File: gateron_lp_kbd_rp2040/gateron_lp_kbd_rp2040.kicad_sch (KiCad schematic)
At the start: 241 parts, among them J1 TYPE-C-31-M-12, J2 JST-SH-2 SM02B, Q1 DMG3415U, SW1 KS-33, SW10 KS-33, SW11 KS-33, SW12 KS-33, SW13 KS-33, SW14 KS-33, SW15 KS-33, SW16 KS-33, SW17 KS-33, SW18 KS-33, SW19 KS-33, SW2 KS-33, SW20 KS-33, SW21 KS-33, SW22 KS-33, SW23 KS-33, SW24 KS-33, SW25 KS-33, SW26 KS-33, SW27 KS-33, SW28 KS-33, SW29 KS-33, SW3 KS-33, SW30 KS-33, SW31 KS-33, SW32 KS-33, SW33 KS-33, SW34 KS-33, SW35 KS-33, SW36 KS-33, SW37 KS-33, SW38 KS-33, SW39 KS-33, SW4 KS-33, SW40 KS-33, SW41 KS-33, SW42 KS-33, SW43 KS-33, SW44 KS-33, SW45 KS-33, SW46 KS-33, SW47 KS-33, SW48 KS-33, SW49 KS-33, SW5 KS-33, SW50 KS-33, SW51 KS-33, SW52 KS-33, SW53 KS-33, SW54 2U, SW55 KS-33, SW56 KS-33, SW57 KS-33, SW58 KS-33, SW59 KS-33, SW6 KS-33, SW60 RESET, SW61 BOOTSEL (VERIFY), SW62 PWR MSK-12C02, SW7 KS-33, SW8 KS-33, SW9 KS-33, U1 RP2040, U2 MCP73831-2ACI/OT, U3 AP2112K-3.3, U4 USBLC6-2SC6, U5 W25Q16JVUXIQ, U6 CYW43439, U7 SN74AHCT1G125DBVR, Y1 12MHz, Y2 37.4MHz

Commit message: Verify RGB power budget against the SK6812MINI-E datasheet, fix 2 gaps
Replaced the vague "several amps" claim with a calculated figure: the
datasheet (Dongguan Opsco, SPC/SK6812MINI-E Rev. 02) confirms 12mA/channel
x 3 channels = 36mA/LED at full white, so 59 LEDs = 2.12A max -- and
surfaced two things that weren't previously flagged:

- D60 (B5819W Schottky, ~1A average current rating) sits in the VSYS path
  whenever the board is USB-powered, and 2.12A would exceed it by >2x.
  The AP2112K-3.3 LDO mismatch was already documented and correctly
  avoided by feeding the RGB chain from VSYS instead -- but D60 is NOT
  bypassed by that design, and nothing previously checked its rating
  against the real max RGB current.
- SK6812MINI-E's own datasheet specs VDD 3.7-5.5V. VSYS (a single-cell
  Li-ion rail) can sag below 3.7V well within normal discharge range, not
  just as a battery-dead edge case. The level shifter (verified
  separately) only guarantees the DIN logic threshold is met -- it says
  nothing about whether the LEDs' own supply voltage stays in spec.

Also added a local 100nF decoupling cap per LED (C100-C158, +4mm offset,
clear of the LED's own courtyard and the switch courtyards above/below),
matching the SK6812MINI-E datasheet's own typical application circuit
("even the capacitance between beads is essential") -- an earlier version
had only one bulk cap (C19) at the chain's start, 59 LEDs away from the
far end.

Verified via kicad-happy analyzers: zero new courtyard collisions, zero
schematic label collisions across the full file, only pre-existing/
expected findings remain.

Co-Authored-By: Claude Sonnet 5 <noreply@anthropic.com>
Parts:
- added C100, C101, C102, C103, C104, C105, C106, C107, C108, C109, C110, C111, C112, C113, C114, C115, C116, C117, C118, C119, C120, C121, C122, C123, C124, C125, C126, C127, C128, C129, C130, C131, C132, C133, C134, C135, C136, C137, C138, C139, C140, C141, C142, C143, C144, C145, C146, C147, C148, C149, C150, C151, C152, C153, C154, C155, C156, C157, C158: 100n, kbd:RC_0603, symbol kbd:C_kbd
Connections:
- net GND: now also C100.2, C101.2, C102.2, C103.2, C104.2, C105.2, C106.2, C107.2, C108.2, C109.2, C110.2, C111.2, C112.2, C113.2, C114.2, C115.2, C116.2, C117.2, C118.2, C119.2, C120.2, C121.2, C122.2, C123.2, C124.2, C125.2, C126.2, C127.2, C128.2, C129.2, C130.2, C131.2, C132.2, C133.2, C134.2, C135.2, C136.2, C137.2, C138.2, C139.2, C140.2, C141.2, C142.2, C143.2, C144.2, C145.2, C146.2, C147.2, C148.2, C149.2, C150.2, C151.2, C152.2, C153.2, C154.2, C155.2, C156.2, C157.2, C158.2
- net VSYS: now also C100.1, C101.1, C102.1, C103.1, C104.1, C105.1, C106.1, C107.1, C108.1, C109.1, C110.1, C111.1, C112.1, C113.1, C114.1, C115.1, C116.1, C117.1, C118.1, C119.1, C120.1, C121.1, C122.1, C123.1, C124.1, C125.1, C126.1, C127.1, C128.1, C129.1, C130.1, C131.1, C132.1, C133.1, C134.1, C135.1, C136.1, C137.1, C138.1, C139.1, C140.1, C141.1, C142.1, C143.1, C144.1, C145.1, C146.1, C147.1, C148.1, C149.1, C150.1, C151.1, C152.1, C153.1, C154.1, C155.1, C156.1, C157.1, C158.1
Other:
- note added: "RGB power budget (calculated from the SK6812MINI-E datasheet, 12mA/channel x 3 x 59 LEDs = 2.12A max at full white): fed from VSYS, NOT the 3.3V LDO (AP2112K-3.3 isn't remotely rated for this). D60 (B5819W, ~1A avg rating) IS in this path when USB-powered and WOULD be exceeded by 2.12A -- firmware must cap brightness/concurrent-on count well below full-white-all-keys regardless of power source. A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"
- note removed: "RGB chain fed from VSYS (unregulated battery/USB), NOT the 3.3V LDO -- 59 LEDs at full white can draw several amps, far beyond the AP2112K-3.3's rating. Firmware must cap brightness/concurrent-on count. Level shifter keeps DIN threshold margin safe across the VSYS voltage range."

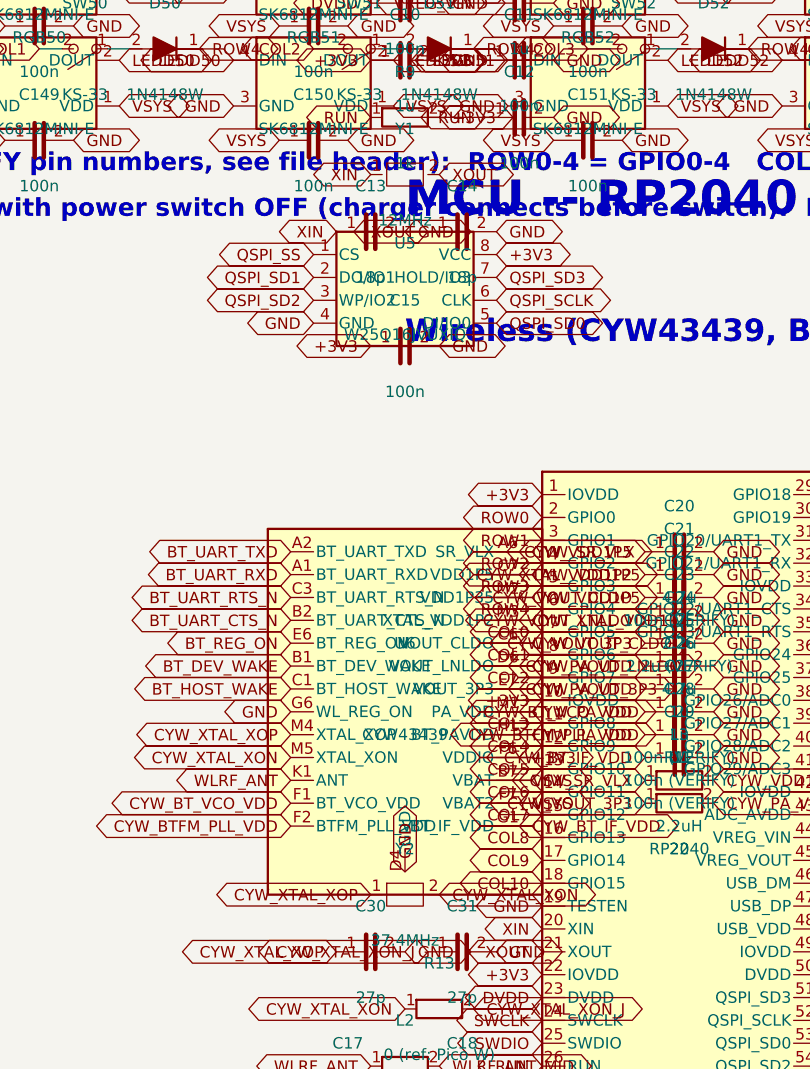
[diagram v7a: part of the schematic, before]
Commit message: Add RP2040 board routing engine, reverse-mount LED redesign, and 3D models
- New route_kbd_rp2040.py: deterministic + A*-hybrid autorouter for the
  RP2040 variant. Hand-routes the congested ROW/COL matrix fanout and
  QSPI north strip net-by-net (verified against the real clearance
  checker), falls back to generic A* elsewhere, and heals remaining
  gaps in a final pass.
- Redesigned the per-key RGB LED footprint (fp_sk6812mini) to a real
  reverse-mount part on B.Cu with a light-transmission cutout, matching
  a verified KiCad reference footprint instead of a hand-derived one.
- Added 3D models to ~15 footprints across both board variants (via
  add_3d.py for the ESP32 variant, inline `model()` blocks for RP2040)
  and synced datasheets for real part verification.
- Fixed several real bugs surfaced while routing: VSYS's per-LED
  routing referenced the wrong pin after the LED footprint redesign
  (silently trying to via into GND on all 59 LEDs); the matching
  per-LED decoupling caps sat in the ~0mm gap between the LED's own
  cutout and the next row's switch leg hole; C33 was placed closer to
  BOOTSEL's through-hole pad than any trace could legally clear;
  BOOTSEL's own switch had two same-named leg pads that were never
  wired together; VBAT_SENSE's escape route was getting walled off by
  whichever of XIN/XOUT happened to route first.
- Board currently routes cleanly except for a known cluster of nets
  (+3V3, DVDD, QSPI_SCLK/SD2/SD3, RGB_GPIO, USB_DM/DP, VREG_VIN) all
  bottlenecked by the same over-saturated escape corridor next to U1 --
  next up for a dedicated deterministic-routing pass.

Co-Authored-By: Claude Sonnet 5 <noreply@anthropic.com>
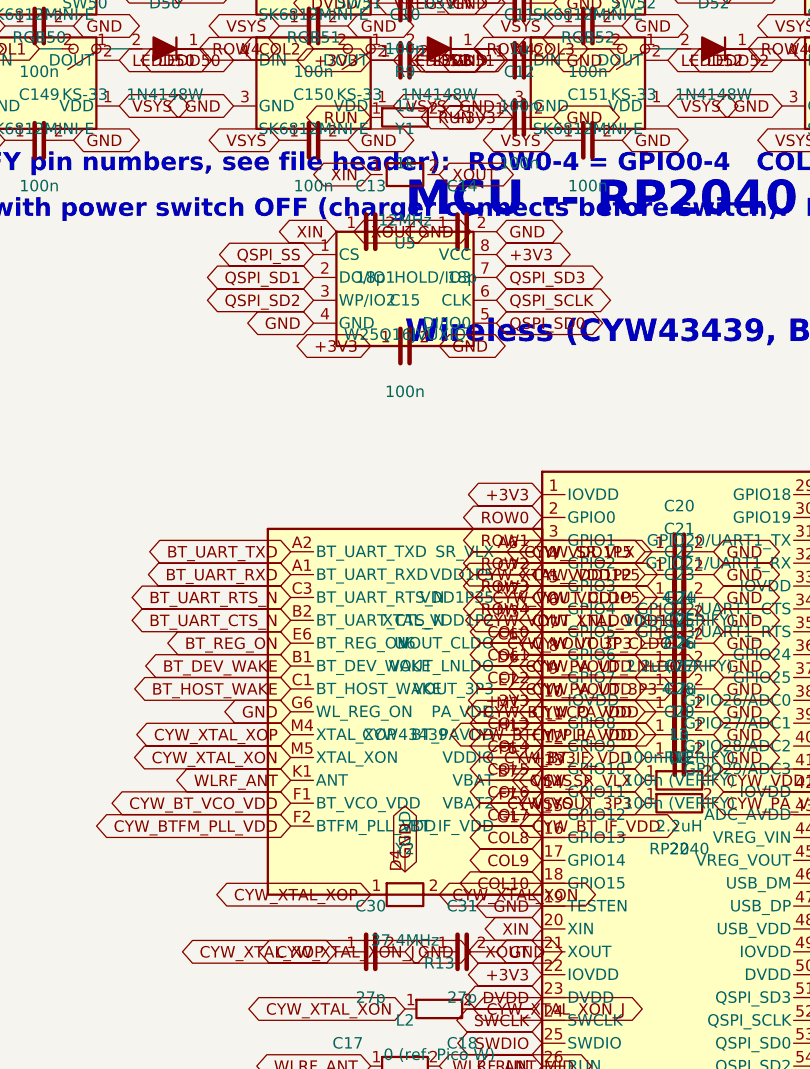
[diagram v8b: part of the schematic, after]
